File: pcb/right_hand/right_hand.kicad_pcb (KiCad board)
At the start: 2 copper layers, 160 x 110 mm, 116 parts, among them J0 UJ20-C-H-G-SMT-P16-TR, U0 SW_Push

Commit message: Soft link right hand to primary copy
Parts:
- moved D_{NUM}1 7.60 mm to (158.4, 58.2), turned to -90 degrees
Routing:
- net Net-(D_{NUM}1-A): track 130.1 -> 142.5 mm
- net /Control/Right_Columns2: track 68.8 -> 65.1 mm
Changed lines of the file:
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@@
 	(footprint "Diode_SMD:D_SOD-323_HandSoldering"
 		(layer "B.Cu")
-		(at 158.4 50.6 90)
+		(at 158.4 58.2 -90)
 		(descr "SOD-323")
 		(tags "SOD-323")
 		(property "Reference" "D_{NUM}1"
-			(at 4.4 -0.2 270)
+			(at 0.2 -1.8 90)
 			(layer "B.SilkS")
 			(effects
@@
 		)
 		(property "Value" "1N4148WX-TP"
-			(at 0.1 -1.9 270)
+			(at 0.1 -1.9 90)
 			(layer "B.Fab")
 			(hide yes)
@@
 		)
 		(property "Datasheet" "https://www.mccsemi.com/pdf/Products/1N4148WX(SOD-323).pdf"
-			(at 0 0 270)
+			(at 0 0 90)
 			(unlocked yes)
 			(layer "B.Fab")
@@
 		)
 		(property "Description" "75V 0.15A Fast Switching Diode, SOD-123"
-			(at 0 0 270)
+			(at 0 0 90)
 			(unlocked yes)
 			(layer "B.Fab")
@@
 		)
 		(property "Sim.Device" "D"
-			(at 0 0 270)
+			(at 0 0 90)
 			(unlocked yes)
 			(layer "B.Fab")
@@
 		)
 		(property "Sim.Pins" "1=K 2=A"
-			(at 0 0 270)
+			(at 0 0 90)
 			(unlocked yes)
 			(layer "B.Fab")
@@
 		(attr smd)
 		(fp_line
-			(start -2.01 -0.85)
-			(end 1.25 -0.85)
+			(start -2.01 0.85)
+			(end 1.25 0.85)
 			(stroke
 				(width 0.12)
@@
 		)
 		(fp_line
-			(start -2.01 0.85)
-			(end 1.25 0.85)
+			(start -2.01 -0.85)
+			(end 1.25 -0.85)
 			(stroke
 				(width 0.12)
@@
 		)
 		(fp_line
-			(start -2 -0.95)
-			(end 2 -0.95)
+			(start -2 0.95)
+			(end 2 0.95)
 			(stroke
 				(width 0.05)
@@
 		)
 		(fp_line
-			(start 2 0.95)
-			(end 2 -0.95)
+			(start -2 0.95)
+			(end -2 -0.95)
 			(stroke
 				(width 0.05)
@@
 		)
 		(fp_line
-			(start -2 0.95)
-			(end -2 -0.95)
+			(start 2 0.95)
+			(end 2 -0.95)
 			(stroke
 				(width 0.05)
@@
 		)
 		(fp_line
-			(start -2 0.95)
-			(end 2 0.95)
+			(start -2 -0.95)
+			(end 2 -0.95)
 			(stroke
 				(width 0.05)
@@
 		)
 		(fp_line
-			(start 0.9 -0.7)
-			(end -0.9 -0.7)
+			(start -0.9 0.7)
+			(end 0.9 0.7)
 			(stroke
 				(width 0.1)
@@
 		)
 		(fp_line
-			(start -0.9 -0.7)
-			(end -0.9 0.7)
+			(start 0.9 0.7)
+			(end 0.9 -0.7)
 			(stroke
 				(width 0.1)
@@
 		)
 		(fp_line
-			(start 0.2 -0.35)
-			(end -0.3 0)
+			(start -0.3 0.35)
+			(end -0.3 -0.35)
 			(stroke
 				(width 0.1)
@@
 		)
 		(fp_line
-			(start 0.2 0)
-			(end 0.45 0)
+			(start 0.2 0.35)
+			(end 0.2 -0.35)
 			(stroke
 				(width 0.1)
@@
 		(fp_line
 			(start -0.3 0)
-			(end -0.5 0)
+			(end 0.2 0.35)
 			(stroke
 				(width 0.1)
@@
 		(fp_line
 			(start -0.3 0)
-			(end 0.2 0.35)
+			(end -0.5 0)
 			(stroke
 				(width 0.1)
@@
 		)
 		(fp_line
-			(start 0.2 0.35)
-			(end 0.2 -0.35)
+			(start 0.2 0)
+			(end 0.45 0)
 			(stroke
 				(width 0.1)
@@
 		)
 		(fp_line
-			(start -0.3 0.35)
-			(end -0.3 -0.35)
+			(start 0.2 -0.35)
+			(end -0.3 0)
 			(stroke
 				(width 0.1)
@@
 		)
 		(fp_line
-			(start 0.9 0.7)
-			(end 0.9 -0.7)
+			(start -0.9 -0.7)
+			(end -0.9 0.7)
 			(stroke
 				(width 0.1)
@@
 		)
 		(fp_line
-			(start -0.9 0.7)
-			(end 0.9 0.7)
+			(start 0.9 -0.7)
+			(end -0.9 -0.7)
 			(stroke
 				(width 0.1)
@@
 		)
 		(fp_text user "${REFERENCE}"
-			(at 4.4 -0.2 270)
+			(at 0.2 -1.8 90)
 			(layer "B.Fab")
 			(effects
@@
 		)
 		(pad "1" smd roundrect
-			(at -1.25 0 90)
+			(at -1.25 0 270)
 			(size 1 1)
 			(layers "B.Cu" "B.Mask" "B.Paste")
@@
 		)
 		(pad "2" smd roundrect
-			(at 1.25 0 90)
+			(at 1.25 0 270)
 			(size 1 1)
 			(layers "B.Cu" "B.Mask" "B.Paste")
@@
 	)
 	(gr_text "*"
-		(at 157.6 65.4 90)
+		(at 158.6 65.4 90)
 		(layer "B.SilkS")
 		(effects
@@
 	)
 	(gr_text "*"
-		(at 158.6 53.4 90)
+		(at 158.6 55.6 90)
 		(layer "B.SilkS")
 		(effects
@@
 	)
 	(segment
-		(start 159.09 51.96)
-		(end 159.16 51.96)
-		(width 0.2)
-		(layer "F.Cu")
-		(net 25)
-	)
-	(segment
 		(start 146.39 51.96)
 		(end 159.09 51.96)
@@
 	)
 	(segment
+		(start 158.369 66.6782)
+		(end 160 65.0472)
+		(width 0.2)
+		(layer "B.Cu")
+		(net 32)
+	)
+	(segment
+		(start 160 58.55)
+		(end 160 65.0472)
+		(width 0.2)
+		(layer "B.Cu")
+		(net 32)
+	)
+	(segment
 		(start 160.2 98.8)
 		(end 160.2 87.3982)
@@
 	)
 	(segment
-		(start 158.369 66.6782)
-		(end 158.369 51.881)
-		(width 0.2)
-		(layer "B.Cu")
-		(net 32)
-	)
-	(segment
-		(start 158.369 51.881)
-		(end 158.4 51.85)
+		(start 158.4 56.95)
+		(end 160 58.55)
 		(width 0.2)
 		(layer "B.Cu")
@@
 	)
 	(segment
-		(start 158.4 49.35)
-		(end 162.55 49.35)
-		(width 0.2)
-		(layer "B.Cu")
-		(net 33)
-	)
-	(segment
 		(start 129.88 62.12)
 		(end 142.58 49.42)
@@
 	)
 	(segment
-		(start 152.74 49.42)
-		(end 158.33 49.42)
-		(width 0.2)
-		(layer "B.Cu")
-		(net 33)
-	)
-	(segment
 		(start 222.59 74.82)
 		(end 203.54 74.82)
@@
 	)
 	(segment
-		(start 108.29 62.12)
-		(end 127.34 62.12)
+		(start 175.32 62.12)
+		(end 162.62 49.42)
 		(width 0.2)
 		(layer "B.Cu")
@@
 	)
 	(segment
-		(start 175.32 62.12)
-		(end 162.55 49.35)
+		(start 108.29 62.12)
+		(end 127.34 62.12)
 		(width 0.2)
 		(layer "B.Cu")
@@
 	)
 	(segment
-		(start 158.33 49.42)
-		(end 158.4 49.35)
+		(start 152.74 53.79)
+		(end 152.74 49.42)
 		(width 0.2)
 		(layer "B.Cu")
@@
 		(width 0.2)
 		(layer "B.Cu")
+		(net 33)
+	)
+	(segment
+		(start 158.4 59.45)
+		(end 152.74 53.79)
+		(width 0.2)
+		(layer "B.Cu")
+		(net 33)
+	)
+	(segment
+		(start 152.74 49.42)
+		(end 162.62 49.42)
+		(width 0.2)
+		(layer "B.Cu")

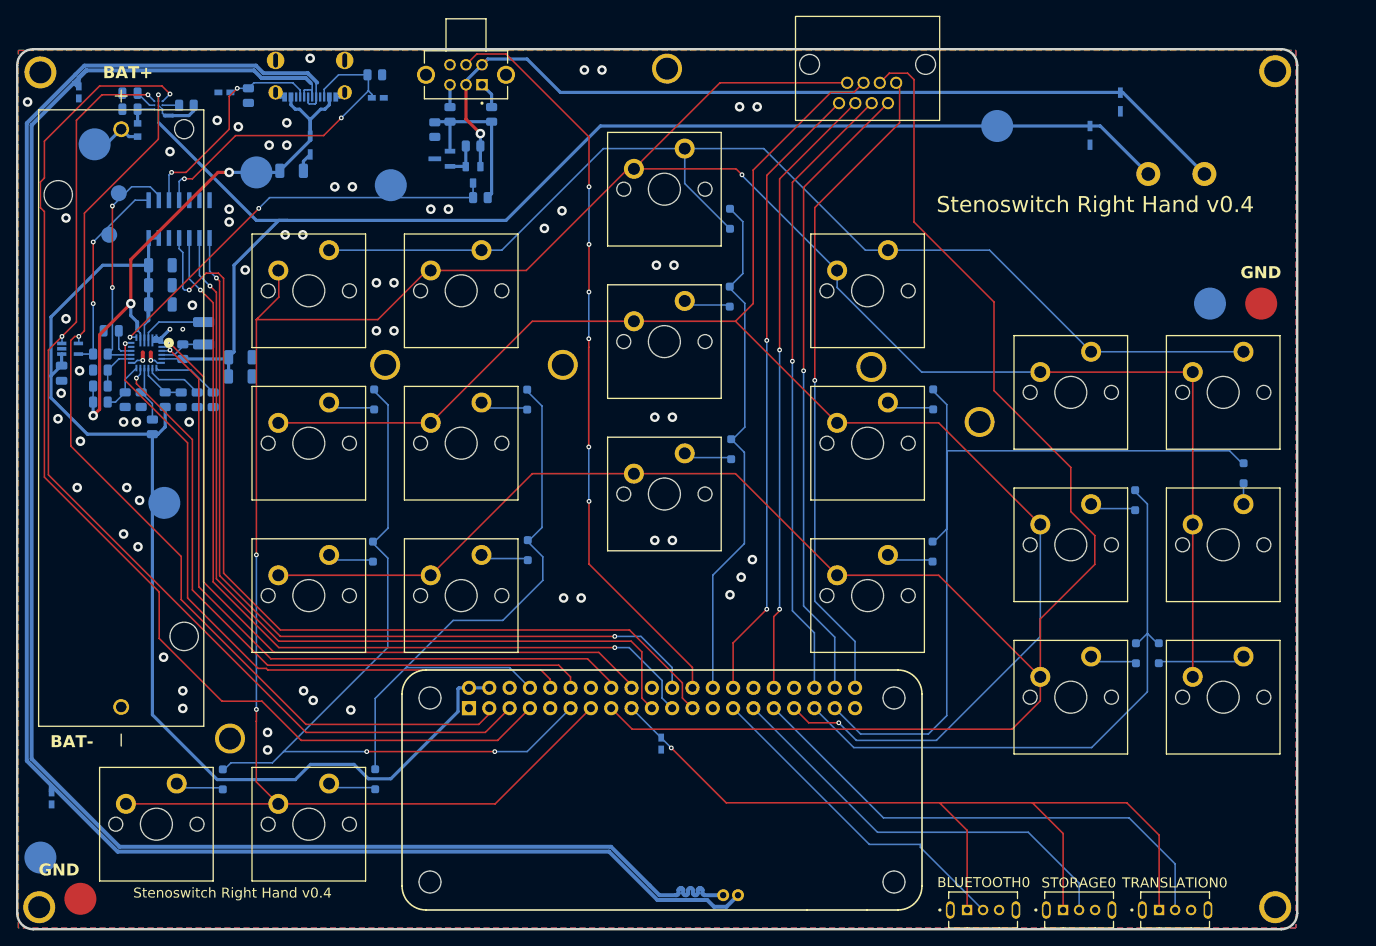
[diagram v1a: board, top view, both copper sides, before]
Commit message: Adjust right hand mounts, testpoints
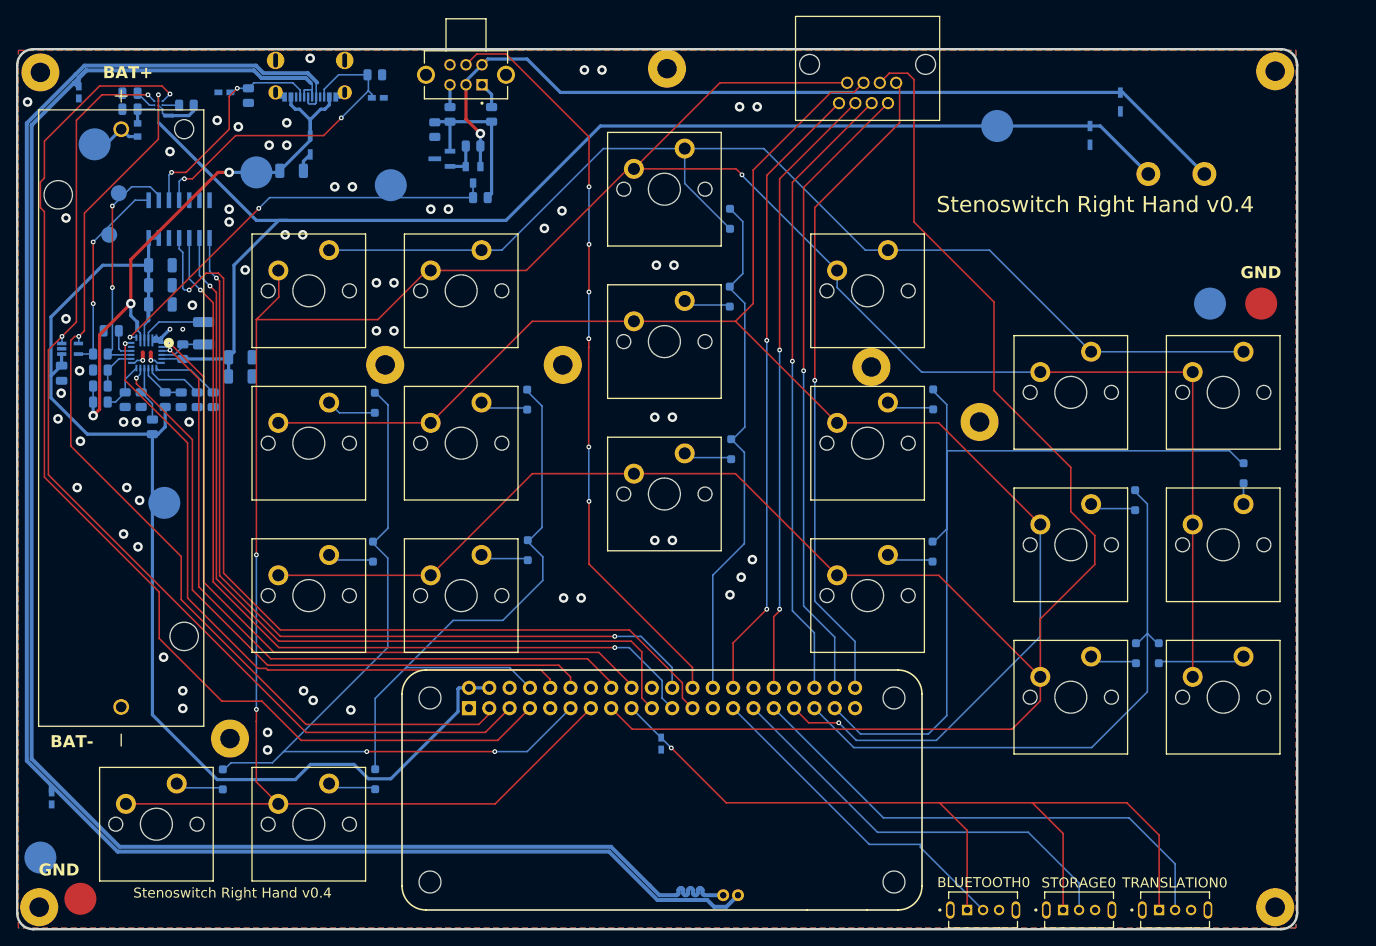
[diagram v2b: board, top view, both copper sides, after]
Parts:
- moved D_{AS}2 0.43 mm to (114.0, 81.2)
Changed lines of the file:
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@@
 		(pad "" thru_hole circle
 			(at 0 0 180)
-			(size 3.75 3.75)
-			(drill 2.75)
+			(size 4.7625 4.7625)
+			(drill 2.4384)
 			(layers "*.Cu" "*.Mask")
 			(remove_unused_layers no)
@@
 		(pad "" thru_hole circle
 			(at 0 0 180)
-			(size 3.75 3.75)
-			(drill 2.75)
+			(size 4.7625 4.7625)
+			(drill 2.4384)
 			(layers "*.Cu" "*.Mask")
 			(remove_unused_layers no)
 			(net 14 "GND")
+			(zone_connect 2)
 		)
 		(embedded_fonts no)
@@
 			(layers "B.Cu" "B.Mask")
 			(net 14 "GND")
+			(zone_connect 2)
 		)
 		(embedded_fonts no)
@@
 		(pad "" thru_hole circle
 			(at 0 0 180)
-			(size 3.75 3.75)
-			(drill 2.75)
+			(size 4.7625 4.7625)
+			(drill 2.4384)
 			(layers "*.Cu" "*.Mask")
 			(remove_unused_layers no)
 			(net 14 "GND")
+			(zone_connect 2)
 		)
 		(embedded_fonts no)
@@
 		(pad "" thru_hole circle
 			(at 0 0 180)
-			(size 4 4)
-			(drill 2.75)
+			(size 4.7625 4.7625)
+			(drill 2.4384)
 			(layers "*.Cu" "*.Mask")
 			(remove_unused_layers no)
 			(net 14 "GND")
+			(zone_connect 2)
 		)
 		(embedded_fonts no)
@@
 		(pad "" thru_hole circle
 			(at 0 0 180)
-			(size 3.75 3.75)
-			(drill 2.75)
+			(size 4.7625 4.7625)
+			(drill 2.4384)
 			(layers "*.Cu" "*.Mask")
 			(remove_unused_layers no)
 			(net 14 "GND")
+			(zone_connect 2)
 		)
 		(embedded_fonts no)
@@
 		(pad "" thru_hole circle
 			(at 0 0 180)
-			(size 4 4)
-			(drill 2.75)
+			(size 4.7625 4.7625)
+			(drill 2.4384)
 			(layers "*.Cu" "*.Mask")
 			(remove_unused_layers no)
 			(net 14 "GND")
+			(zone_connect 2)
 		)
 		(embedded_fonts no)
@@
 		(pad "" thru_hole circle
 			(at 0 0 180)
-			(size 3.75 3.75)
-			(drill 2.75)
+			(size 4.7625 4.7625)
+			(drill 2.4384)
 			(layers "*.Cu" "*.Mask")
 			(remove_unused_layers no)
 			(net 14 "GND")
+			(zone_connect 2)
 		)
 		(embedded_fonts no)
@@
 		(pad "" thru_hole circle
 			(at 0 0 180)
-			(size 4 4)
-			(drill 2.75)
+			(size 4.7625 4.7625)
+			(drill 2.4384)
 			(layers "*.Cu" "*.Mask")
 			(remove_unused_layers no)
 			(net 14 "GND")
+			(zone_connect 2)
 		)
 		(embedded_fonts no)
@@
 		(pad "" thru_hole circle
 			(at 0 0 180)
-			(size 3.75 3.75)
-			(drill 2.75)
+			(size 4.7625 4.7625)
+			(drill 2.4384)
 			(layers "*.Cu" "*.Mask")
 			(remove_unused_layers no)
 			(net 14 "GND")
+			(zone_connect 2)
 		)
 		(embedded_fonts no)
@@
 			(layers "B.Cu" "B.Mask")
 			(net 14 "GND")
+			(zone_connect 2)
 		)
 		(embedded_fonts no)
@@
 		(pad "" thru_hole circle
 			(at 0 0 180)
-			(size 4 4)
-			(drill 2.75)
+			(size 4.7625 4.7625)
+			(drill 2.4384)
 			(layers "*.Cu" "*.Mask")
 			(remove_unused_layers no)
 			(net 14 "GND")
+			(zone_connect 2)
 		)
 		(embedded_fonts no)
@@
 			(layers "F.Cu" "F.Mask")
 			(net 14 "GND")
+			(zone_connect 2)
 		)
 		(embedded_fonts no)
@@
 	(footprint "Diode_SMD:D_SOD-323_HandSoldering"
 		(layer "B.Cu")
-		(at 113.919 80.7806 -90)
+		(at 114 81.2 -90)
 		(descr "SOD-323")
 		(tags "SOD-323")
@@
 			(layers "F.Cu" "F.Mask")
 			(net 14 "GND")
+			(zone_connect 2)
 		)
 		(embedded_fonts no)
@@
 	)
 	(segment
-		(start 108.9506 81.8306)
-		(end 108.29 81.17)
+		(start 114 82.45)
+		(end 109.57 82.45)
 		(width 0.2)
 		(layer "B.Cu")
@@
 	)
 	(segment
-		(start 113.919 81.8306)
-		(end 108.9506 81.8306)
+		(start 109.57 82.45)
+		(end 108.29 81.17)
 		(width 0.2)
 		(layer "B.Cu")
@@
 	)
 	(segment
+		(start 114.1384 79.95)
+		(end 115.6462 81.4578)
+		(width 0.2)
+		(layer "B.Cu")
+		(net 26)
+	)
+	(segment
 		(start 129 124.8)
 		(end 133.04 124.8)
@@
 	)
 	(segment
-		(start 115.6462 81.4578)
-		(end 113.919 79.7306)
+		(start 114 79.95)
+		(end 114.1384 79.95)
 		(width 0.2)
 		(layer "B.Cu")

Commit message: Relabel right hand
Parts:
- removed J0: UJ20-C-H-G-SMT-P16-TR, snap_magic_footprints:SAMESKY_UJ20-C-H-G-SMT-P16-TR
- added USB0: USB4105-GF-A, Connector_USB:USB_C_Receptacle_GCT_USB4105-xx-A_16P_TopMnt_Horizontal, B.Cu at (105.9, 39.3)
- BAT_Fuse0: value ERB-RE1R00V -> 2.5 A
- BAT_MIN0: value DMG2305 -> DMG2305UX-7
- CR3: value ESD321 -> ESD321DYAR
- RLIM_{L}0: value MCP40D19T -> MCP40D19T-104E_LT
- VBAT_PASS0: value TLV431 -> TLV431BIDBZR
- renumbered BLUETOOTH0 to BLUETOOTH, TSD05 to CR6, TSD05 to CR7, STORAGE0 to STORAGE, TRANSLATION0 to TRANSLATION, USB_Default_Power_CC2 to USB_Default_Power_CC1, USB_Default_Power_CC1 to USB_Default_Power_CC2
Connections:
- BLUETOOTH pad SH1: (no net) -> GND
- BLUETOOTH pad SH2: (no net) -> GND
- STORAGE pad SH1: (no net) -> GND
- STORAGE pad SH2: (no net) -> GND
- STORE_EN0 pad S1: (no net) -> GND
- STORE_EN0 pad S2: (no net) -> GND
- TRANSLATION pad SH1: (no net) -> GND
- TRANSLATION pad SH2: (no net) -> GND
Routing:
- net /Interface/Battery/V_{BUS}: track 71.4 -> 70.6 mm
- net /Control/Data_N: track 222.6 -> 223.2 mm
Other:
- board text added: "10k(2)"
- board text added: "22uF(3)"
- board text added: "BLUETOOTH"
- board text added: "BQ27427"
- board text added: "DMG2305"
- board text added: "MCP40D19T"
- board text added: "STORAGE"
- board text added: "TLV431"
- board text added: "TRANSLATION"
- board text added: "TSD05"
- board text added: "USB"
